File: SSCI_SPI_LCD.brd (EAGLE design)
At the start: 110 x 100 mm, 33 parts, among them IC3 74LVC541_RGY, X1 PHA-1X08SG, X2 PHA-1X08SG

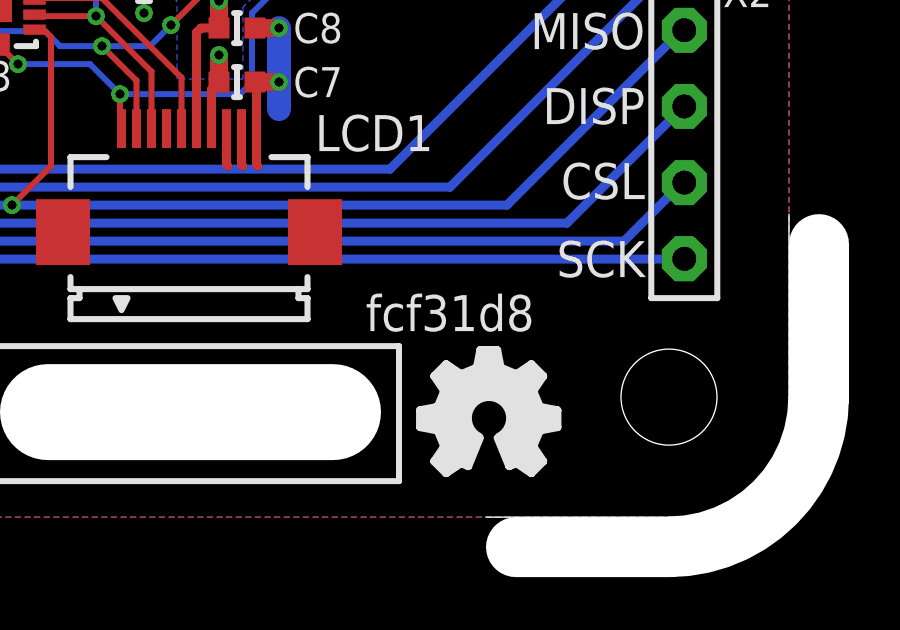
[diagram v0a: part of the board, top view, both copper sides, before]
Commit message: update git revision; remove unnecessary tRestrict
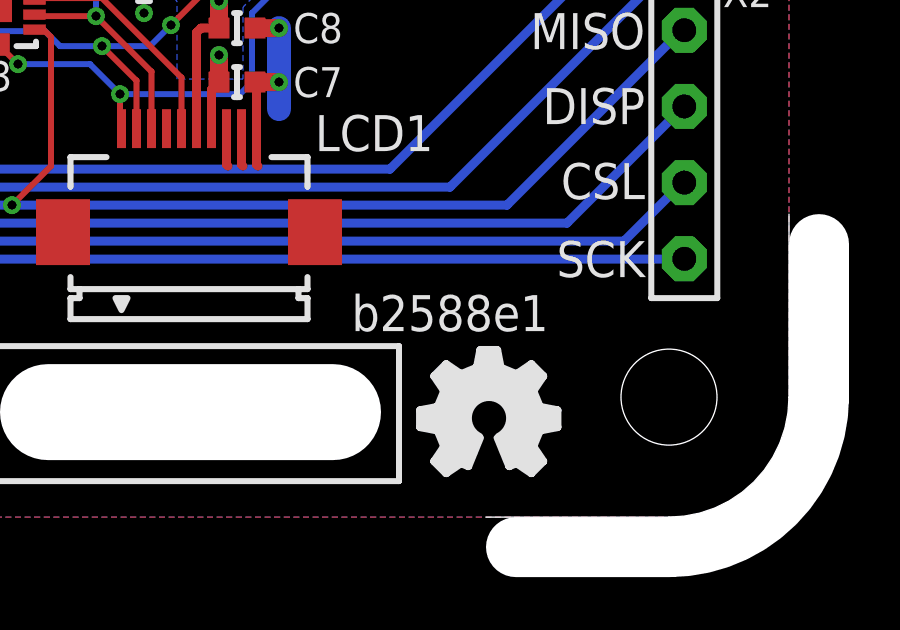
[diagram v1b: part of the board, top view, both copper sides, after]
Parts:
- GIT1: value fcf31d8 -> b2588e1
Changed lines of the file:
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@@
 <wire x1="32" y1="23.6" x2="32" y2="22.3" width="0" layer="41"/>
 <wire x1="30.5" y1="25.5" x2="30.5" y2="23.8" width="0" layer="41"/>
-<wire x1="19.8" y1="28.5" x2="20.3" y2="28.5" width="0" layer="41"/>
 <wire x1="22.8" y1="30" x2="22.8" y2="30.5" width="0" layer="41"/>
 <wire x1="21.9" y1="30" x2="21.9" y2="30.5" width="0" layer="41"/>
@@
 <attribute name="NOT_COMPONENT" value="YES" x="14" y="14" size="1.778" layer="27" rot="R270" display="off"/>
 </element>
-<element name="GIT1" library="git-revision" package="GIT-REVISION_1.2" value="fcf31d8" x="38.7" y="16.8">
+<element name="GIT1" library="git-revision" package="GIT-REVISION_1.2" value="b2588e1" x="38.7" y="16.8">
 <attribute name="NOT_COMPONENT" value="YES" x="38.7" y="16.8" size="1.778" layer="27" display="off"/>
 </element>

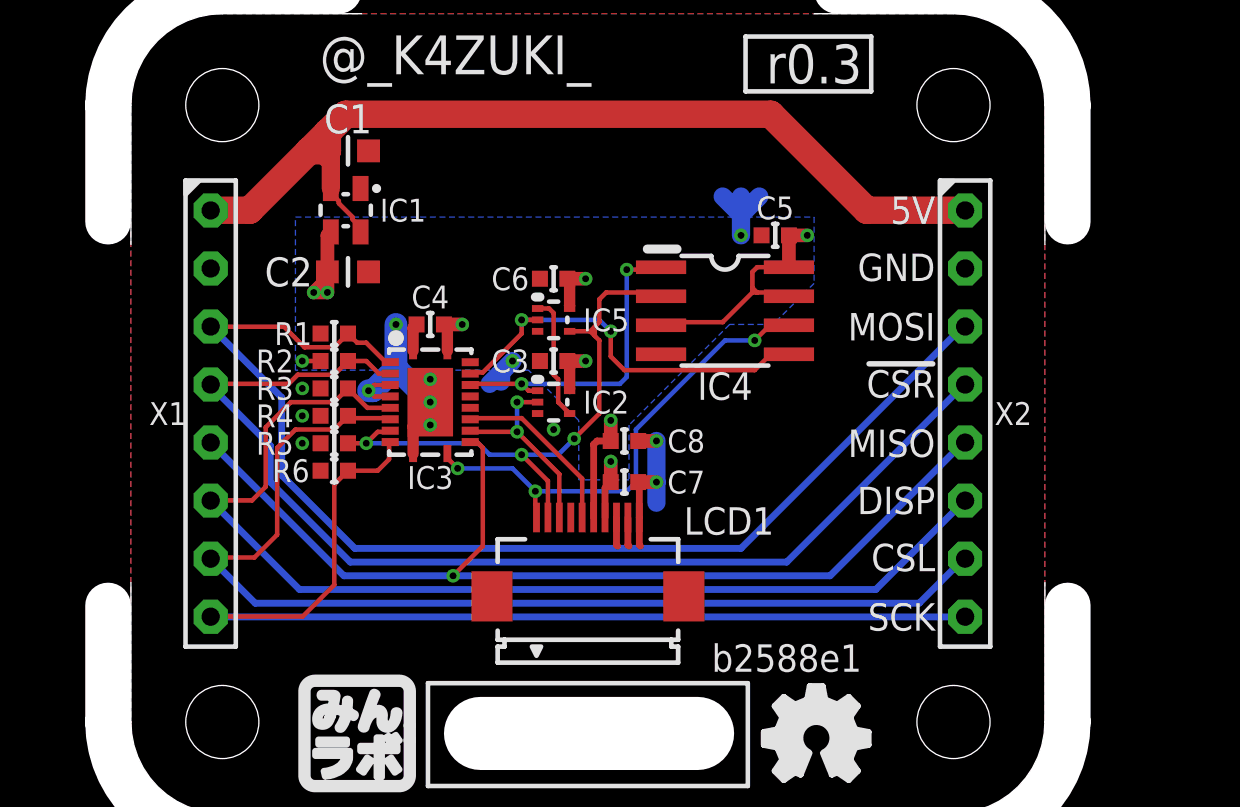
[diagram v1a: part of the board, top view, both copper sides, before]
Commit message: pin header distance get 200mil narrower
- 1300mil -> 1100mil
- matches with "standard" breadboard
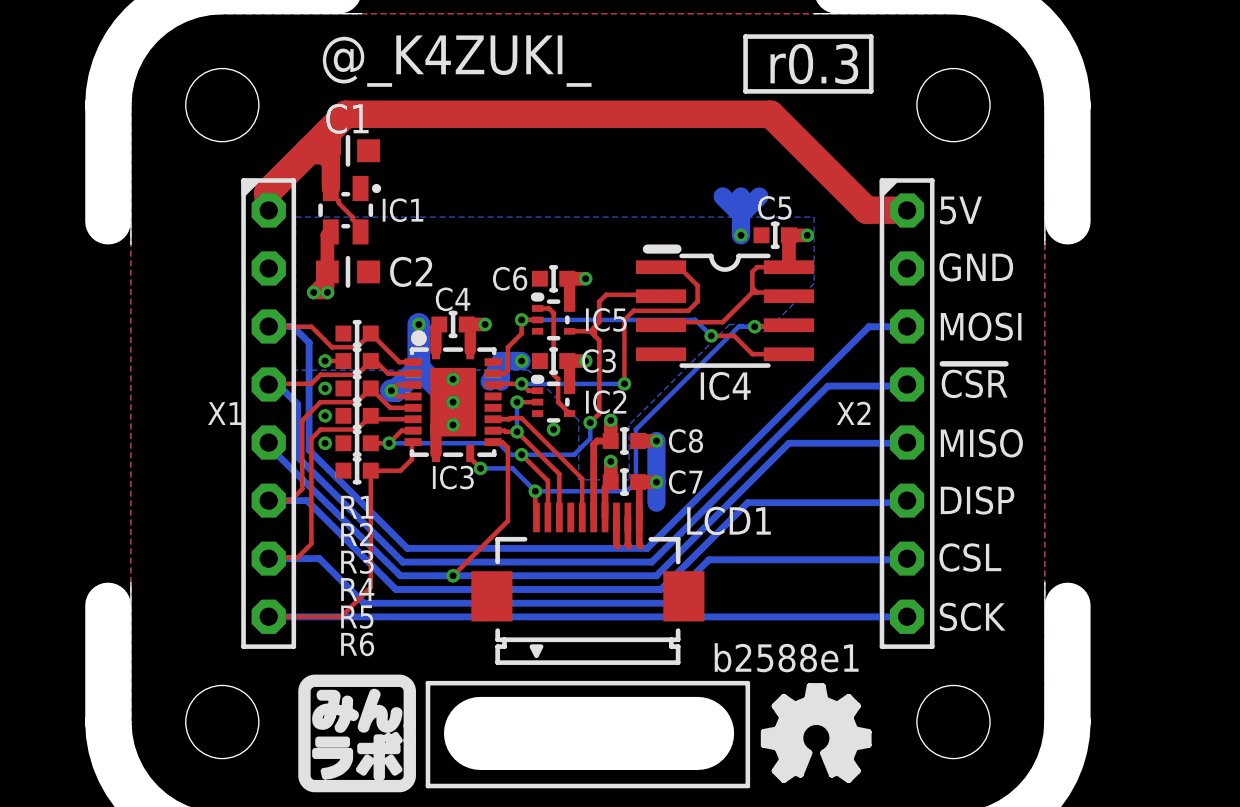
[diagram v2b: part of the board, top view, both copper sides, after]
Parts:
- moved X1 2.54 mm to (16.0, 27.5)
- moved X2 2.54 mm to (44.0, 27.5)
- moved C4 1.00 mm to (24.1, 31.4)
- moved IC3 1.00 mm to (24.1, 28.0)
- moved R1 1.00 mm to (19.9, 31.0)
- moved R2 1.00 mm to (19.9, 29.8)
- moved R3 1.00 mm to (19.9, 28.6)
- moved R4 1.00 mm to (19.9, 27.4)
- moved R5 1.00 mm to (19.9, 26.2)
- moved R6 1.00 mm to (19.9, 25.0)
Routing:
- net DISP: track 48.0 -> 41.7 mm
- net SCK: track 47.0 -> 40.9 mm
- net !CSR!: track 48.9 -> 42.9 mm
- net CSL: track 47.4 -> 41.3 mm
- net MOSI: track 52.1 -> 46.3 mm
- net 5V: track 43.4 -> 38.9 mm
- net MISO: track 44.6 -> 40.3 mm
- net MOSI-: track 17.8 -> 16.2 mm
- net !CSR!-: track 14.3 -> 15.6 mm
- net GND: track 26.4 -> 27.4 mm
- net DISP-: track 7.72 -> 6.72 mm
- net CSL-: track 8.79 -> 7.79 mm
- net SCK-: track 21.3 -> 20.3 mm
- net MISO-: track 26.0 -> 25.2 mm

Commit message: update library
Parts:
- GIT1: value b2588e1 -> f4c890b
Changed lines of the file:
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@@
 <layer number="49" name="Reference" color="7" fill="1" visible="no" active="yes"/>
 <layer number="50" name="dxf" color="7" fill="1" visible="no" active="yes"/>
-<layer number="51" name="tDocu" color="7" fill="1" visible="no" active="yes"/>
+<layer number="51" name="tDocu" color="7" fill="1" visible="yes" active="yes"/>
 <layer number="52" name="bDocu" color="7" fill="1" visible="yes" active="yes"/>
 <layer number="53" name="tGND_GNDA" color="7" fill="9" visible="no" active="no"/>
@@
 <attribute name="NOT_COMPONENT" value="YES" x="14" y="14" size="1.778" layer="27" rot="R270" display="off"/>
 </element>
-<element name="GIT1" library="git-revision" package="GIT-REVISION_1.2" value="b2588e1" x="38.7" y="16.8">
+<element name="GIT1" library="git-revision" package="GIT-REVISION_1.2" value="f4c890b" x="38.7" y="16.8">
 <attribute name="NOT_COMPONENT" value="YES" x="38.7" y="16.8" size="1.778" layer="27" display="off"/>
 </element>
@@
 <attribute name="NAME" x="19.5" y="40.4" size="1.27" layer="25" font="vector" ratio="15" align="center"/>
 <attribute name="VALUE" x="19.4" y="39" size="1.27" layer="27" font="vector" ratio="15" align="center"/>
+<attribute name="SMD_PAD" value="2" x="19.5" y="39" size="1.778" layer="27" display="off"/>
 </element>
 <element name="C2" library="mylib" package="CR_1608" value="" x="19.5" y="33.7" smashed="yes">
@@
 <attribute name="NAME" x="22.3" y="33.7" size="1.27" layer="25" font="vector" ratio="15" align="center"/>
 <attribute name="VALUE" x="19.4" y="33.7" size="1.27" layer="27" font="vector" ratio="15" align="center"/>
+<attribute name="SMD_PAD" value="2" x="19.5" y="33.7" size="1.778" layer="27" display="off"/>
 </element>
 <element name="C3" library="mylib" package="C0402" value="" x="28.5" y="29.8" smashed="yes" rot="R180">
@@
 <attribute name="NAME" x="30.5" y="29.8" size="1" layer="25" font="vector" ratio="20" rot="R180" align="center"/>
 <attribute name="VALUE" x="28.5" y="29.8" size="1" layer="27" font="vector" rot="R180" align="center"/>
+<attribute name="SMD_PAD" value="2" x="28.5" y="29.8" size="1.778" layer="27" rot="R180" display="off"/>
 </element>
 <element name="C4" library="mylib" package="C0402" value="" x="24.1" y="31.4" smashed="yes" rot="R180">
@@
 <attribute name="NAME" x="24.1" y="32.5" size="1" layer="25" font="vector" ratio="20" rot="R180" align="center"/>
 <attribute name="VALUE" x="24.1" y="31.4" size="1" layer="27" font="vector" rot="R180" align="center"/>
+<attribute name="SMD_PAD" value="2" x="24.1" y="31.4" size="1.778" layer="27" rot="R180" display="off"/>
 </element>
 <element name="C5" library="mylib" package="C0402" value="" x="38.2" y="35.3" smashed="yes" rot="R180">
@@
 <attribute name="NAME" x="38.2" y="36.5" size="1" layer="25" font="vector" ratio="20" rot="R180" align="center"/>
 <attribute name="VALUE" x="38.2" y="35.3" size="1" layer="27" font="vector" rot="R180" align="center"/>
+<attribute name="SMD_PAD" value="2" x="38.2" y="35.3" size="1.778" layer="27" rot="R180" display="off"/>
 </element>
 <element name="C6" library="mylib" package="C0402" value="" x="28.5" y="33.4" smashed="yes" rot="R180">
@@
 <attribute name="NAME" x="26.6" y="33.4" size="1" layer="25" font="vector" ratio="20" rot="R180" align="center"/>
 <attribute name="VALUE" x="28.5" y="33.4" size="1" layer="27" font="vector" rot="R180" align="center"/>
+<attribute name="SMD_PAD" value="2" x="28.5" y="33.4" size="1.778" layer="27" rot="R180" display="off"/>
 </element>
 <element name="R2" library="mylib" package="C0402" value="" x="19.9" y="29.8" smashed="yes">
@@
 <attribute name="NAME" x="19.9" y="22.2" size="1" layer="25" font="vector" ratio="20" align="center"/>
 <attribute name="VALUE" x="19.9" y="29.8" size="1" layer="27" font="vector" align="center"/>
+<attribute name="SMD_PAD" value="2" x="19.9" y="29.8" size="1.778" layer="27" display="off"/>
 </element>
 <element name="R1" library="mylib" package="C0402" value="" x="19.9" y="31" smashed="yes">
@@
 <attribute name="VALUE" x="19.9" y="31" size="1" layer="27" font="vector" align="center"/>
 <attribute name="NOT_COMPONENT" value="YES" x="19.9" y="31" size="1.778" layer="27" display="off"/>
+<attribute name="SMD_PAD" value="2" x="19.9" y="31" size="1.778" layer="27" display="off"/>
 </element>
 <element name="R5" library="mylib" package="C0402" value="" x="19.9" y="26.2" smashed="yes">
@@
 <attribute name="NAME" x="19.9" y="18.6" size="1" layer="25" font="vector" ratio="20" align="center"/>
 <attribute name="VALUE" x="19.9" y="26.2" size="1" layer="27" font="vector" align="center"/>
+<attribute name="SMD_PAD" value="2" x="19.9" y="26.2" size="1.778" layer="27" display="off"/>
 </element>
 <element name="R3" library="mylib" package="C0402" value="" x="19.9" y="28.6" smashed="yes">
@@
 <attribute name="NAME" x="19.9" y="21" size="1" layer="25" font="vector" ratio="20" align="center"/>
 <attribute name="VALUE" x="19.9" y="28.6" size="1" layer="27" font="vector" align="center"/>
+<attribute name="SMD_PAD" value="2" x="19.9" y="28.6" size="1.778" layer="27" display="off"/>
 </element>
 <element name="R4" library="mylib" package="C0402" value="" x="19.9" y="27.4" smashed="yes">
@@
 <attribute name="NAME" x="19.9" y="19.8" size="1" layer="25" font="vector" ratio="20" align="center"/>
 <attribute name="VALUE" x="19.9" y="27.4" size="1" layer="27" font="vector" align="center"/>
+<attribute name="SMD_PAD" value="2" x="19.9" y="27.4" size="1.778" layer="27" display="off"/>
 </element>
 <element name="R6" library="mylib" package="C0402" value="" x="19.9" y="25" smashed="yes">
@@
 <attribute name="NAME" x="19.9" y="17.4" size="1" layer="25" font="vector" ratio="20" align="center"/>
 <attribute name="VALUE" x="19.9" y="25" size="1" layer="27" font="vector" align="center"/>
+<attribute name="SMD_PAD" value="2" x="19.9" y="25" size="1.778" layer="27" display="off"/>
 </element>
 <element name="C7" library="mylib" package="C0402" value="" x="31.6" y="24.5" smashed="yes">
@@
 <attribute name="NAME" x="34.3" y="24.5" size="1" layer="25" font="vector" ratio="20" align="center"/>
 <attribute name="VALUE" x="31.6" y="24.5" size="1" layer="27" font="vector" align="center"/>
+<attribute name="SMD_PAD" value="2" x="31.6" y="24.5" size="1.778" layer="27" display="off"/>
 </element>
 <element name="C8" library="mylib" package="C0402" value="" x="31.6" y="26.3" smashed="yes">
@@
 <attribute name="NAME" x="34.3" y="26.3" size="1" layer="25" font="vector" ratio="20" align="center"/>
 <attribute name="VALUE" x="31.6" y="26.3" size="1" layer="27" font="vector" align="center"/>
+<attribute name="SMD_PAD" value="2" x="31.6" y="26.3" size="1.778" layer="27" display="off"/>
 </element>
 <element name="ICON2" library="mylib" package="ICON_OSHW" value="" x="40" y="13.3">

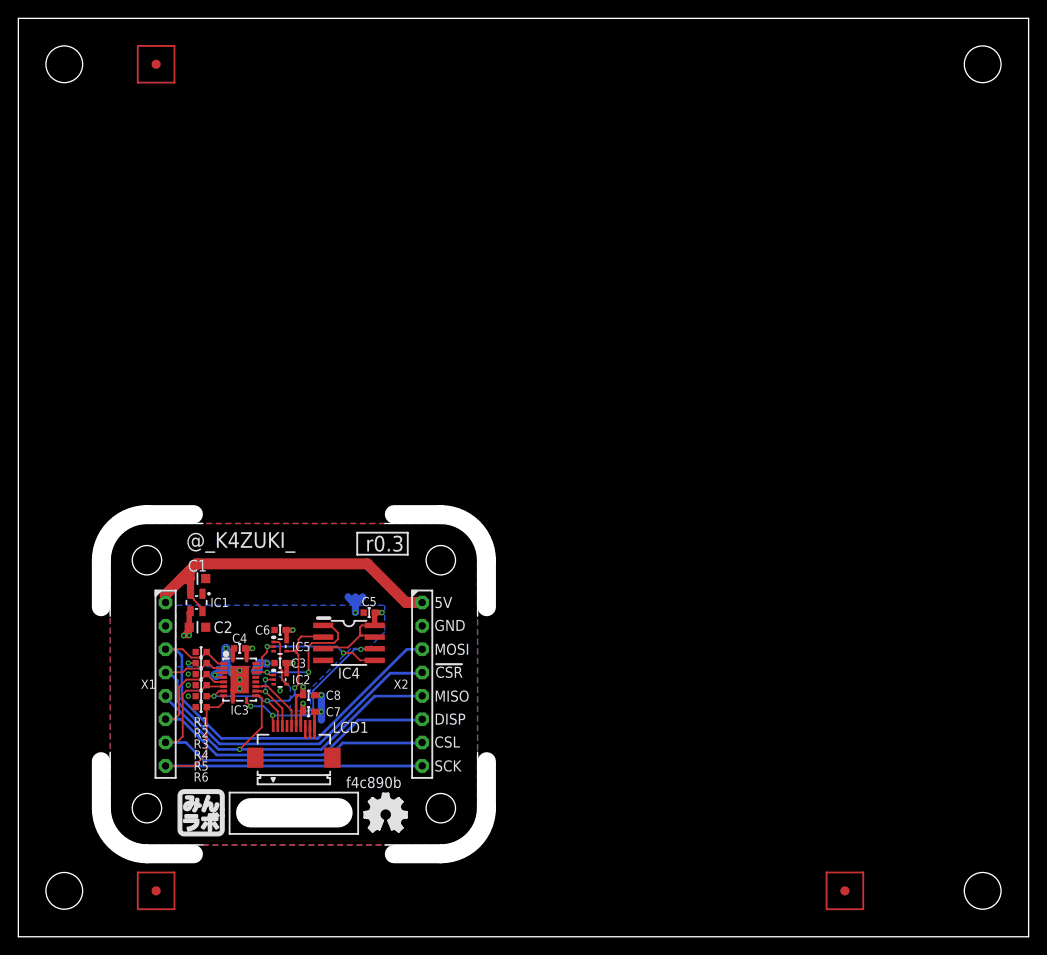
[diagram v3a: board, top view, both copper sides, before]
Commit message: outline resized
- no more corner screw holes
- still panelized in 110x100(3x2)
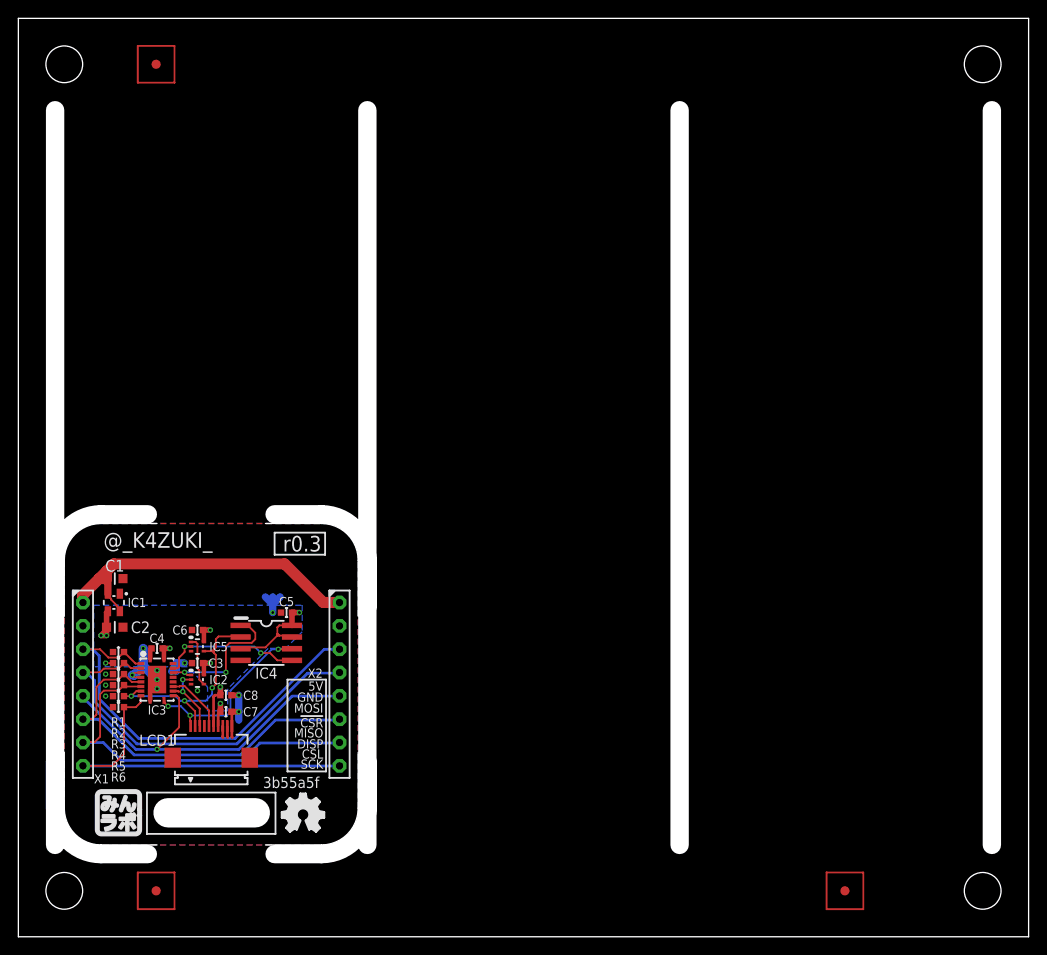
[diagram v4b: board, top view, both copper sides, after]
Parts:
- GIT1: value f4c890b -> 3b55a5f
- P1, P2, P3, P4: device mylib:PCB_CORNER -> mylib:PCB_CORNER_NH
- moved P1 13.0 mm to (33.0, 14.0)
- moved P2 13.0 mm to (33.0, 41.0)
- moved C5 9.00 mm to (29.2, 35.3)
- moved GIT1 9.00 mm to (29.7, 16.8)
- moved C4 9.00 mm to (15.1, 31.4)
- moved IC3 9.00 mm to (15.1, 28.0)
- moved C1 9.00 mm to (10.5, 39.0)
- moved C2 9.00 mm to (10.5, 33.7)
- moved C3 9.00 mm to (19.5, 29.8)
- moved C6 9.00 mm to (19.5, 33.4)
- moved C7 9.00 mm to (22.6, 24.5)
- moved C8 9.00 mm to (22.6, 26.3)
- moved IC2 9.00 mm to (19.5, 28.0)
- moved IC4 9.00 mm to (27.0, 32.0)
- moved IC5 9.00 mm to (19.5, 31.6)
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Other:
- outline, holes or cut-outs redrawn
